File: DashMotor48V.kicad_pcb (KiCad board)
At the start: 6 copper layers, 71.8 x 70.7 mm, 81 parts, among them CN3(OUT)1 XT30(2+2)PB-M.G.B, CN3(OUT)2 XT30(2+2)PB-M.G.B, J1 BM07B-SRSS-TB, J2 BM07B-SRSS-TB, Q1 FDMS039N08B, Q2 FDMS039N08B, Q3 FDMS039N08B, Q4 FDMS039N08B, Q5 FDMS039N08B, Q6 FDMS039N08B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

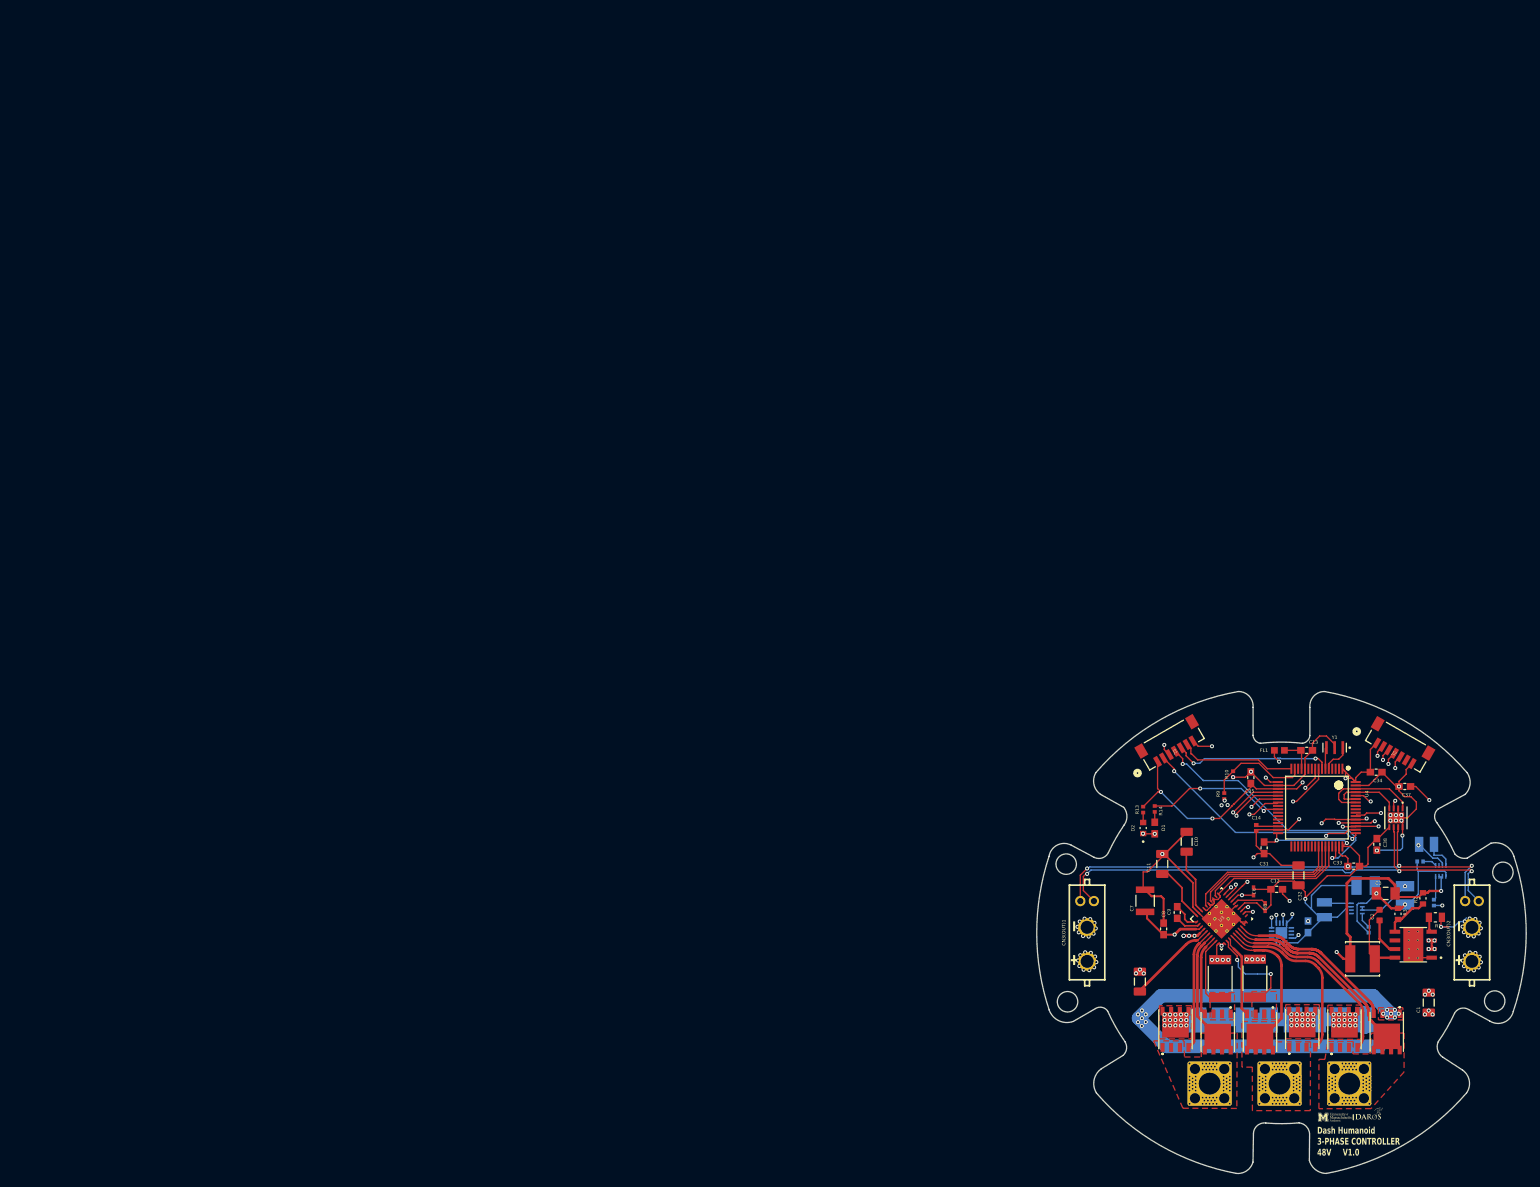
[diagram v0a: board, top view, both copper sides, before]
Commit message: formalize footprint and port
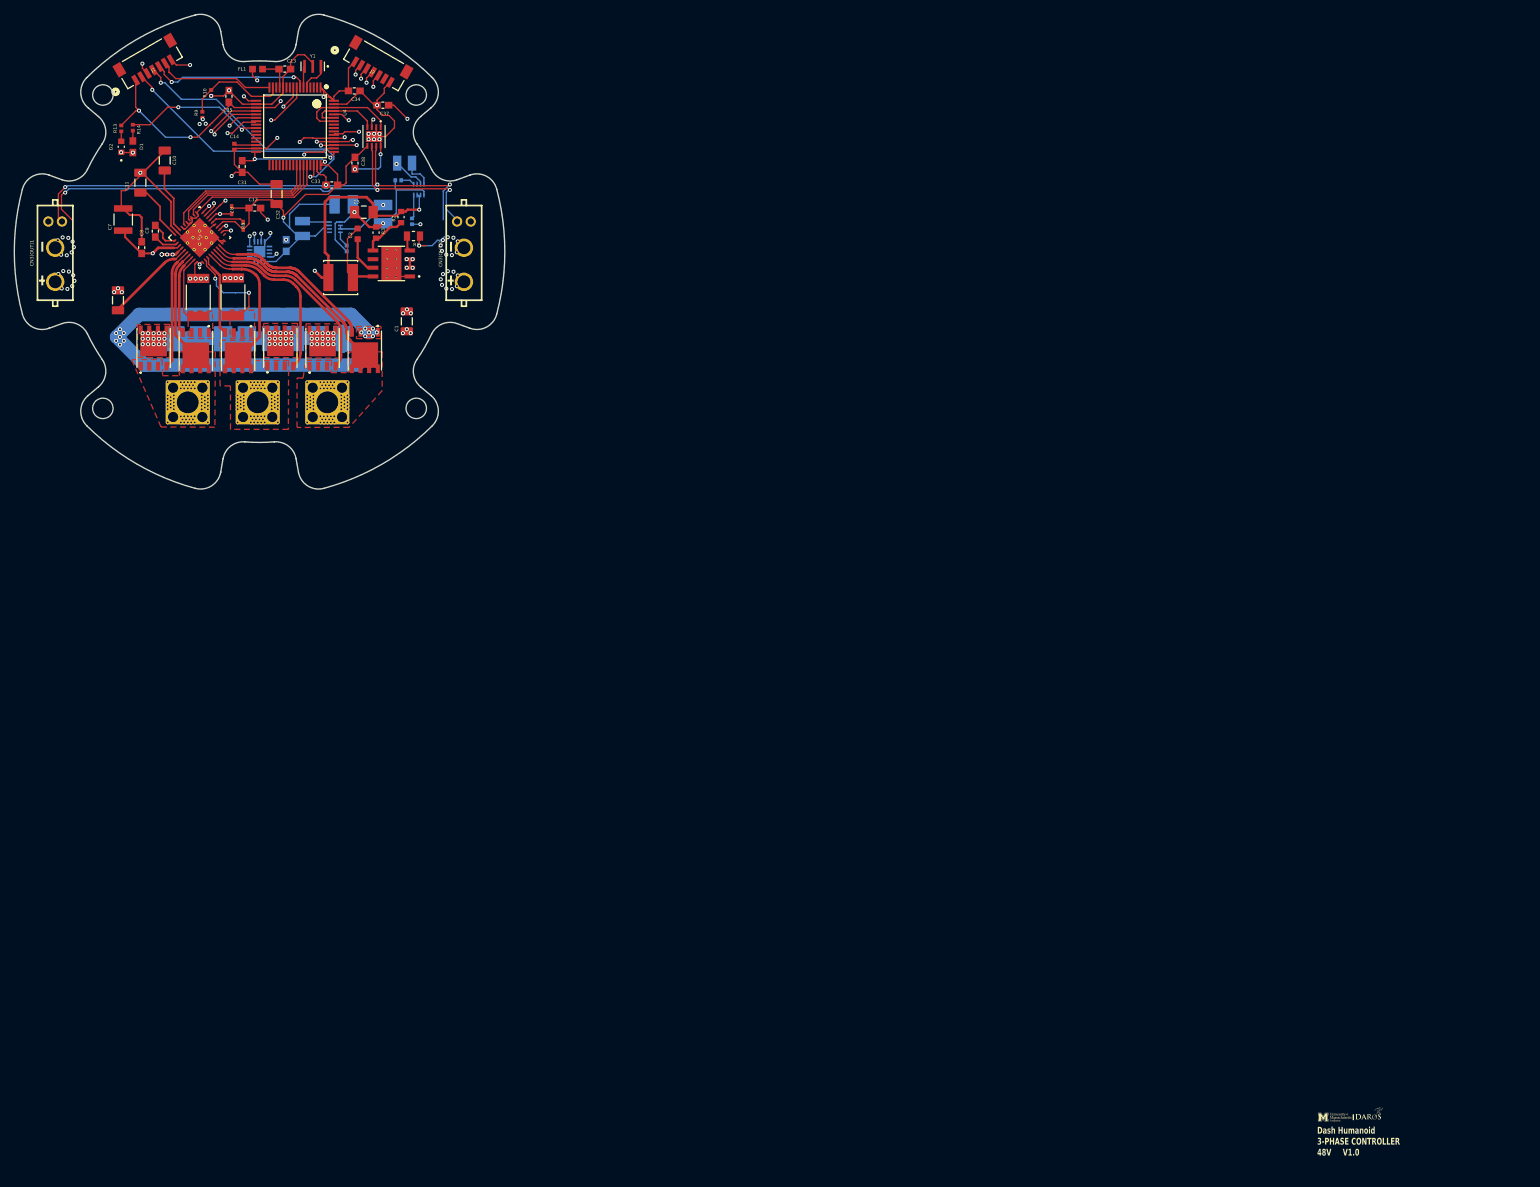
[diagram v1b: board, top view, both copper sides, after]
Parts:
- moved CN3(OUT)1 181.4 mm to (-30.0, 0.00)
- moved C1 180.3 mm to (21.6, 10.2)
- moved C10 180.3 mm to (-13.9, -13.4)
- moved C11 180.3 mm to (-17.5, -10.1)
- moved C12 180.3 mm to (-0.70, -6.40)
- moved C13 180.3 mm to (3.70, -26.8)
- moved C14 180.3 mm to (-3.70, -15.4)
- moved C15 180.3 mm to (12.2, 15.2)
- moved C16 180.3 mm to (8.70, 15.2)
- moved C17 180.3 mm to (5.20, 15.2)
- moved C18 180.3 mm to (1.70, 15.2)
- moved C19 180.3 mm to (1.70, 10.3)
- moved C2 180.3 mm to (14.4, -2.62)
- moved C20 180.3 mm to (5.20, 10.3)
- moved C21 180.3 mm to (8.70, 10.3)
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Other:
- board size 71.8 x 70.7 mm -> 72 x 69.7 mm

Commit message: keep working on the 2nd version
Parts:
- moved C15 44.8 mm to (-26.8, 37.2)
- moved C16 44.8 mm to (-30.3, 37.2)
- moved C17 44.8 mm to (-33.8, 37.2)
- moved C18 44.8 mm to (-37.3, 37.2)
- moved C19 44.8 mm to (-37.3, 32.4)
- moved C20 44.8 mm to (-33.8, 32.4)
- moved C21 44.8 mm to (-30.3, 32.4)
- moved C30 44.8 mm to (-26.8, 32.4)
- moved C22 31.6 mm to (-32.9, 21.5)
- moved C23 31.6 mm to (-36.4, 21.5)
- moved C24 31.6 mm to (-39.9, 21.5)
- moved C25 31.6 mm to (-43.4, 21.5)
- moved C26 31.6 mm to (-43.4, 16.7)
- moved C27 31.6 mm to (-39.9, 16.7)
- moved C28 31.6 mm to (-36.4, 16.7)
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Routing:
- net GND: track 247.8 -> 171.3 mm, vias 72 -> 90
- net +48V: track 38.8 -> 7.65 mm, vias 82 -> 52
- net /PHASC: vias 0 -> 3
- net /PHASB: vias 0 -> 3
- net /PHASA: vias 0 -> 3
- net /GHC: vias 0 -> 1
- net /GHB: vias 0 -> 1
- net /GHA: vias 0 -> 1
- added copper zone on B.Cu, net +48V
- added copper zone on B.Cu, net GND

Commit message: keep working on 2nd version
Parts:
- moved C15 41.2 mm to (-64.5, 20.7), turned to -90 degrees
- moved C16 34.9 mm to (-61.0, 20.7), turned to -90 degrees
- moved C22 31.8 mm to (-58.8, 39.9)
- moved C23 31.8 mm to (-62.2, 39.9)
- moved C24 31.8 mm to (-65.8, 39.9)
- moved C25 31.8 mm to (-69.2, 39.9)
- moved C17 28.9 mm to (-57.5, 20.7), turned to -90 degrees
- moved C27 26.0 mm to (-51.0, 40.2)
- moved C28 26.0 mm to (-47.5, 40.2)
- moved C29 26.0 mm to (-44.0, 40.2)
- moved C26 25.9 mm to (-54.4, 40.2)
- moved C21 19.1 mm to (-46.2, 21.8), turned to 0 degrees
- moved C30 13.7 mm to (-40.3, 34.7), turned to 0 degrees
- moved L1 10.5 mm to (17.2, -5.25), turned to 90 degrees
- moved R1 10.3 mm to (21.8, 8.00), turned to 0 degrees
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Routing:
- net +12V: track 69.0 -> 10.1 mm, vias 3 -> 7
- net +5V: track 38.5 -> 5.95 mm, vias 4 -> 8
- net GND: track 171.3 -> 151.0 mm, vias 90 -> 59
- net +3.3V: track 151.8 -> 134.3 mm
- net /CAN+: track 74.2 -> 58.1 mm, vias 3 -> 2
- net /CAN-: track 74.3 -> 58.5 mm, vias 3 -> 2
- net Net-(U3-VCP): track 13.5 -> 5.73 mm
- net Net-(VR1-SW): track 11.2 -> 6.30 mm
- net /GHB: track 26.1 -> 21.4 mm, vias 1 -> 0
- net Net-(U3-CPL): track 4.23 -> 0.00 mm
- net /PHASB: track 22.6 -> 18.6 mm, vias 3 -> 0
- net Net-(VR1-RON): track 2.31 -> 6.24 mm
- net Net-(U3-CPH): track 3.75 -> 0.00 mm
- net +48V: track 7.65 -> 3.96 mm, vias 52 -> 80
- net Net-(U3-FAULT_N): track 4.92 -> 1.79 mm
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- added copper zone on B.Cu, net +12V
- added copper zone on F.Cu, net +12V
- added copper zone on B.Cu, net +5V
- added copper zone on In2.Cu, net +5V
- added copper zone on F.Cu, net /GLB
- added copper zone on F.Cu, net /GLC

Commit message: Add files via upload
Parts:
- added ?: , , F.Cu at (3.20, 14.5)
- moved G*** 157.3 mm to (49.2, 13.3)
- moved G*** 157.3 mm to (54.2, 12.8)
- moved C28 75.3 mm to (19.8, 6.53), turned to 180 degrees
- moved C27 70.9 mm to (14.2, 12.3)
- moved C26 70.8 mm to (10.7, 12.3)
- moved C29 70.5 mm to (19.8, 10.2), turned to 180 degrees
- moved C15 62.0 mm to (-3.05, 12.3)
- moved C16 62.0 mm to (0.40, 12.3)
- moved C17 61.9 mm to (3.85, 12.3)
- moved C25 60.5 mm to (-20.5, 4.16), turned to 0 degrees
- moved C23 57.0 mm to (-15.2, 7.79), turned to 180 degrees
- moved C22 56.3 mm to (-15.2, 4.16), turned to 180 degrees
- moved C24 55.5 mm to (-20.5, 7.79), turned to 0 degrees
- moved C21 54.3 mm to (7.30, 12.3), turned to -90 degrees
- moved C30 32.4 mm to (-16.8, 12.3), turned to -90 degrees
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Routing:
- net /CAN+: track 58.1 -> 76.9 mm, vias 2 -> 3
- net /CAN-: track 58.5 -> 77.2 mm, vias 2 -> 3
- net +3.3V: track 134.3 -> 145.6 mm
- net +48V: track 3.96 -> 11.8 mm, vias 80 -> 113
- net +5V: track 5.95 -> 10.0 mm
- net /PHASA: track 19.3 -> 15.3 mm
- net /GLA: track 14.1 -> 10.2 mm
- net /GHA: track 20.6 -> 16.7 mm
- net Net-(U3-CPH): track 0.00 -> 3.75 mm
- net Net-(U3-CPL): track 0.00 -> 3.55 mm
- net Net-(U3-DVDD): track 9.63 -> 6.51 mm
- net /SPA: track 11.7 -> 9.13 mm
- net /GHB: track 21.4 -> 24.0 mm
- net Net-(U1-MODE/S-CONF): track 0.00 -> 2.02 mm
- net /PHASB: track 18.6 -> 20.6 mm
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- added copper zone on In2.Cu, net +12V
- added copper zone on In3.Cu, net +12V
- added copper zone on F.Cu, net /GHA
- added copper zone on F.Cu, net /GHB
- added copper zone on F.Cu, net /GHC
- added copper zone on F.Cu, net /GLA
- added copper zone on F.Cu, net Net-(U3-VCP)
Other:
- board text added: "*"

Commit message: work on 2ndraft
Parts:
- moved R4 11.0 mm to (16.0, -7.60), turned to 180 degrees
- moved U2 9.72 mm to (12.2, -7.20), turned to 90 degrees
- moved C5 9.20 mm to (10.4, 2.60)
- moved R5 7.97 mm to (16.0, -6.00), turned to 180 degrees
- moved L2 7.68 mm to (8.50, -6.19), turned to -90 degrees
- moved C4 3.95 mm to (14.6, -2.86)
- moved C1 3.61 mm to (22.0, 2.94)
- moved R6 3.58 mm to (12.2, -2.43), turned to 90 degrees
- moved L1 3.57 mm to (19.7, -2.70)
- moved VR1 3.40 mm to (26.1, -0.15)
- moved R3 3.38 mm to (27.5, -5.70), turned to 180 degrees
- moved C3 3.28 mm to (15.3, -3.17)
- moved C2 2.83 mm to (24.3, -4.80)
- moved L3 2.31 mm to (6.40, -1.09)
- moved CN3(OUT)2 2.00 mm to (32.0, 0.00)
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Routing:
- net GND: track 150.8 -> 114.9 mm, vias 54 -> 50
- net +3.3V: track 145.6 -> 130.9 mm
- net +5V: track 10.0 -> 5.02 mm, vias 8 -> 2
- net Net-(U1-SW): track 3.17 -> 0.00 mm
- net Net-(VR1-RON): track 7.17 -> 5.08 mm
- net Net-(VR1-FB): track 5.62 -> 7.60 mm
- net Net-(U2-MODE/S-CONF): track 1.45 -> 0.00 mm
- net Net-(U2-FB/VSET): track 1.45 -> 0.00 mm
- net Net-(VR1-SW): track 6.30 -> 7.59 mm
- net /CAN+: track 76.9 -> 76.1 mm
- net /CAN-: track 77.2 -> 77.8 mm
- removed copper zone on B.Cu, net +12V
- removed copper zone on In2.Cu, net +12V
- removed copper zone on In3.Cu, net +12V
- removed copper zone on B.Cu, net +5V
- removed copper zone on In2.Cu, net +5V

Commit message: no error for the 2nd draft
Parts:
- moved C30 33.1 mm to (15.8, 7.10), turned to 0 degrees
- moved R9 26.0 mm to (-19.6, 3.30), turned to 180 degrees
- moved C29 8.37 mm to (18.3, 1.94), turned to -90 degrees
- moved C24 7.48 mm to (-24.9, 1.76), turned to -90 degrees
- moved C28 4.99 mm to (21.8, 1.94), turned to -90 degrees
- moved C7 3.40 mm to (-20.0, -1.32)
- moved C25 2.56 mm to (-21.3, 1.74), turned to -90 degrees
- moved U6 0.72 mm to (17.5, -16.9)
- moved R12 0.62 mm to (-2.30, 8.05)
- moved R4 0.48 mm to (15.7, -8.00)
- moved R5 0.48 mm to (15.7, -6.40)
- moved C22 0.14 mm to (-15.4, 4.16)
- moved C23 0.14 mm to (-15.4, 7.79)
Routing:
- net +12V: track 9.80 -> 54.2 mm, vias 11 -> 12
- net GND: track 114.9 -> 156.8 mm, vias 50 -> 55
- net Net-(U4-PA1): track 15.2 -> 50.6 mm
- net +3.3V: track 130.9 -> 121.5 mm, vias 8 -> 14
- net /TMS: track 39.2 -> 33.1 mm
- net +48V: track 11.8 -> 7.72 mm, vias 113 -> 77
- net /CAN-: track 77.8 -> 74.1 mm, vias 3 -> 2
- net Net-(U1-SW): track 0.00 -> 3.13 mm
- net /MOSI: track 36.9 -> 39.9 mm
- net /MISO: track 34.8 -> 37.5 mm
- net /CS: track 20.5 -> 23.0 mm
- net Net-(U2-MODE/S-CONF): track 0.00 -> 2.34 mm
- net Net-(U2-FB/VSET): track 0.00 -> 2.27 mm
- net /SCK: track 37.0 -> 39.2 mm
- net /CAN_TX: track 14.7 -> 16.2 mm
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- added copper zone on B.Cu, net +12V
- added copper zone on In2.Cu, net +12V
- added copper zone on B.Cu, net +3.3V
- added copper zone on In2.Cu, net +3.3V
- added copper zone on B.Cu, net +5V
- added copper zone on In3.Cu, net +5V

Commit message: minor tweak
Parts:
- moved C32 9.54 mm to (-4.80, -13.1)
- moved C11 3.53 mm to (-15.7, -5.96)
- moved C10 3.41 mm to (-13.3, -5.96)
- moved C14 1.20 mm to (-2.50, -15.4)
- moved R10 0.55 mm to (-6.63, -23.6), turned to 180 degrees
- turned C31 to -90 degrees
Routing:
- net GND: track 156.8 -> 142.8 mm, vias 55 -> 56
- net Net-(U4-PA1): track 50.6 -> 46.5 mm
- net Net-(U3-DVDD): track 6.51 -> 3.20 mm
- net Net-(U3-VGLS): track 8.41 -> 5.51 mm
- net +3.3V: track 121.5 -> 124.4 mm
- net /TMS: track 33.1 -> 30.3 mm
- net Net-(U4-VCAP_1): track 3.28 -> 2.08 mm
- net /I_A: track 27.3 -> 28.1 mm
- net /ENABLE: track 27.5 -> 26.8 mm

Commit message: change color and stuff
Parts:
- added H4: MountingHole, MountingHole:MountingHole_2.2mm_M2_Pad, F.Cu at (23.0, -23.5)
- added H5: MountingHole, MountingHole:MountingHole_2.2mm_M2_Pad, F.Cu at (-23.0, -23.5)
- added H6: MountingHole, MountingHole:MountingHole_2.2mm_M2_Pad, F.Cu at (23.0, 23.5)
- added H7: MountingHole, MountingHole:MountingHole_2.2mm_M2_Pad, F.Cu at (-23.0, 23.5)
- moved G*** 65.4 mm to (-14.2, 29.4)
- moved G*** 65.4 mm to (-9.20, 28.8)
- moved CN3(OUT)1 2.00 mm to (-32.0, 0.00)
- moved J2 1.36 mm to (16.0, -28.0)
- moved C34 0.70 mm to (13.8, -22.9)
- moved J1 0.32 mm to (-16.0, -28.0)
- turned H1 to 0 degrees
- turned H2 to 0 degrees
- turned H3 to 0 degrees
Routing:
- net +3.3V: track 124.4 -> 120.7 mm
- net /CAN+: track 75.9 -> 77.9 mm
- net /NRST: track 24.0 -> 22.5 mm
- net /CAN-: track 74.1 -> 75.5 mm
- net /USART_TX: track 17.3 -> 16.5 mm
- net GND: track 142.8 -> 142.3 mm, vias 56 -> 68
- net +48V: track 7.72 -> 7.67 mm, vias 77 -> 89
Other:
- outline, holes or cut-outs redrawn
- board text added: "Dash Humanoid 48V V0.0"
- board text removed: "Dash Humanoid 3-PHASE CONTROLLER 48V V1.0"
